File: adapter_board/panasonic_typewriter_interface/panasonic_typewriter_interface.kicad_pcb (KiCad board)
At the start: 2 copper layers, 37.3 x 43.7 mm, 21 parts, among them J1 KMDGX-8S-AS, J2 Conn_02x03_Odd_Even, J3 Connector:Conn_01x05_Male, J4 Connector:Conn_01x04_Male, J5 Connector:Conn_01x04_Male, SW1 SW_SPDT

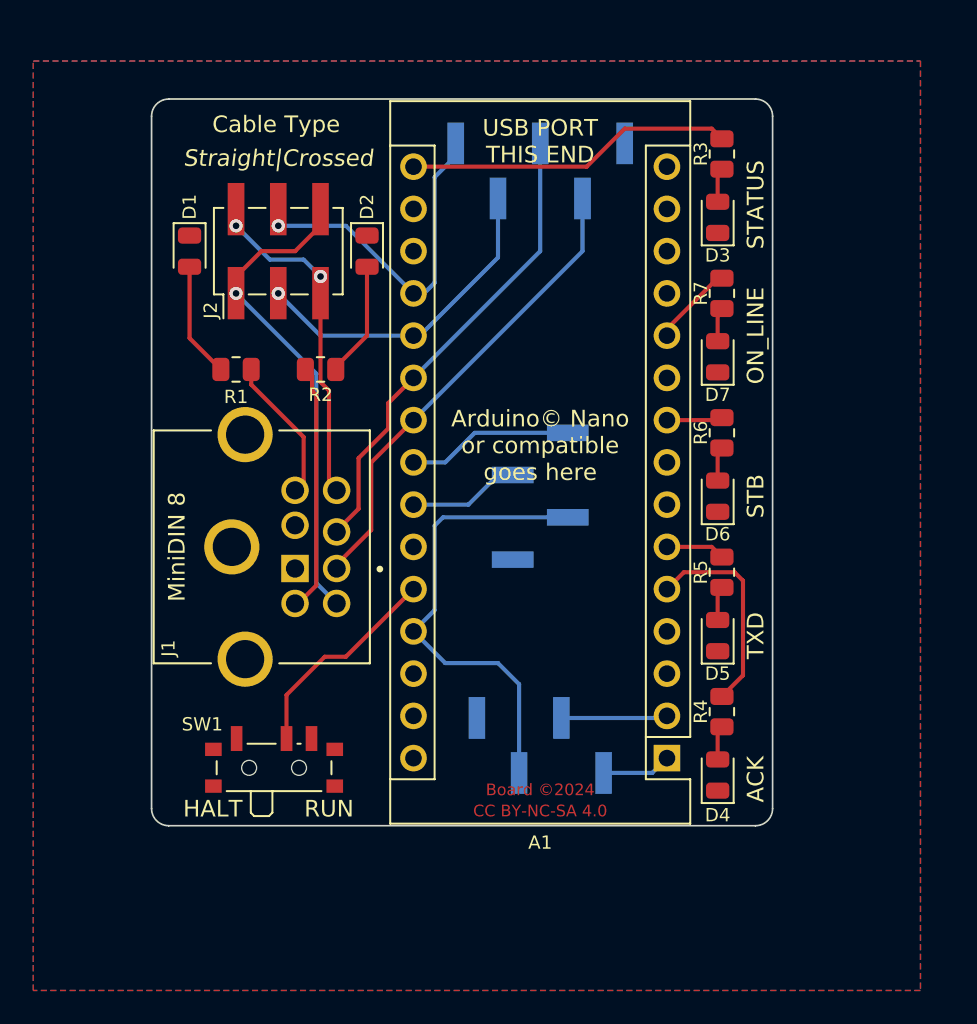
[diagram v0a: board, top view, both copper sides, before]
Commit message: slightly larger board with mounting holes and an extra button
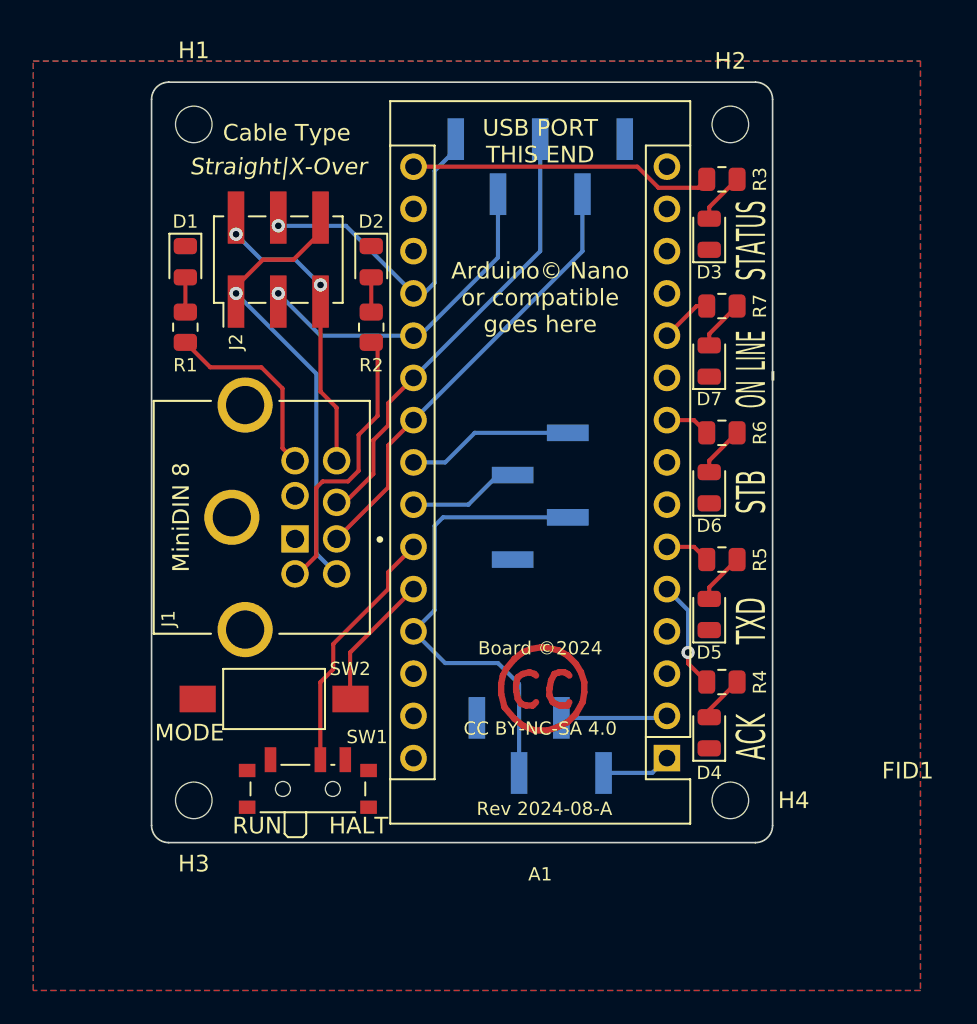
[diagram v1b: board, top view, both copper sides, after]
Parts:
- added FID1: CC, Symbol:Symbol_CreativeCommons_CopperTop_Type2_Small, F.Cu at (144.8, 102.6)
- added H1: MountingHole, MountingHole:MountingHole_2.2mm_M2_DIN965, F.Cu at (124.0, 68.6)
- added H2: MountingHole, MountingHole:MountingHole_2.2mm_M2_DIN965, F.Cu at (156.2, 68.6)
- added H3: MountingHole, MountingHole:MountingHole_2.2mm_M2_DIN965, F.Cu at (124.0, 109.2)
- added H4: MountingHole, MountingHole:MountingHole_2.2mm_M2_DIN965, F.Cu at (156.2, 109.2)
- added SW2: SW_Push, Button_Switch_SMD:SW_SPST_FSMSM, F.Cu at (128.8, 103.1)
- moved R1 3.97 mm to (123.4, 80.8), turned to 90 degrees
- moved R2 3.97 mm to (134.6, 80.8), turned to 90 degrees
- moved D4 2.59 mm to (154.9, 105.2)
- moved SW1 2.40 mm to (130.8, 108.2)
- moved J1 1.78 mm to (126.2, 92.2)
- moved R4 1.78 mm to (155.7, 102.1), turned to 0 degrees
- moved R3 1.52 mm to (155.7, 71.9), turned to 0 degrees
- moved D5 1.37 mm to (154.9, 98.0)
- moved D3 1.14 mm to (154.9, 75.2)
- moved R5 0.76 mm to (155.7, 94.7), turned to 0 degrees
- moved R7 0.76 mm to (155.7, 79.5), turned to 0 degrees
- moved D6 0.72 mm to (154.9, 90.4)
- moved D1 0.68 mm to (123.4, 76.8)
- moved D2 0.68 mm to (134.6, 76.8)
- moved D7 0.57 mm to (154.9, 82.8)
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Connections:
- A1 pad 25: unconnected-(A1-Pad25) -> GO_PIN
- A1 pad 26: GO_PIN -> MODE_PIN
- SW1 pad 1: unconnected-(SW1-Pad1) -> GND
- SW1 pad 3: GND -> unconnected-(SW1-Pad3)
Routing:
- net MODE_PIN: track 0.00 -> 8.19 mm
- net ACK_LED: track 12.7 -> 6.58 mm, vias 0 -> 1
- net Net-(D2-Pad2): track 6.95 -> 2.09 mm
- net Net-(R1-Pad2): track 6.95 -> 2.09 mm
- net +12V_CORRECT: track 8.79 -> 11.6 mm
- net DIN_6_TXD_OR_ON_LINE: track 29.5 -> 27.1 mm
- net +12V_CROSS: track 14.8 -> 17.1 mm
- net DIN_8_TXD_OR_ON_LINE: track 19.6 -> 17.3 mm
- net GO_PIN: track 12.9 -> 15.1 mm
- net ON_LINE_LED: track 4.97 -> 3.13 mm
- net ~{ACK}: track 28.4 -> 26.8 mm
- net STATUS_LED: track 19.7 -> 18.4 mm
- net ~{STB}: track 28.4 -> 27.2 mm
- net Net-(D7-Pad2): track 2.07 -> 3.06 mm
- net Net-(D6-Pad2): track 2.07 -> 3.06 mm
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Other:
- board size 37.3 x 43.7 mm -> 37.3 x 45.7 mm
- board text added: "Arduino Serial Breakout (TTL)"
- board text added: "Cable Type (J2): Move both jumpers on J2 to either STRAIGHT or X-OVER. If connecting KX-R, LEDs D1/D2 show current cable type but jumpers must still be moved to side closest to lit LED."
- board text added: "MODE"
- board text added: "Mounting Holes: Size: M2 Spacing: 40.6mm x 32.6mm"
- board text added: "Rev 2024-08-A"
- board text added: "Straight|X-Over"
- board text added: "Typewriter Signal Breakout (raw)"
- board text removed: "Arduino Serial0 Breakout"
- board text removed: "Cable Type jumper: Move BOTH J2 jumpers to either {dblquote}straight{dblquote} or {dblquote}crossed{dblquote}. If connecting to KX-R, LED will be lit indicating current cable type but jumpers MUST still be moved to side closest to lit LED."
- board text removed: "Straight|Crossed"
- board text removed: "Typewriter Signal Breakout"

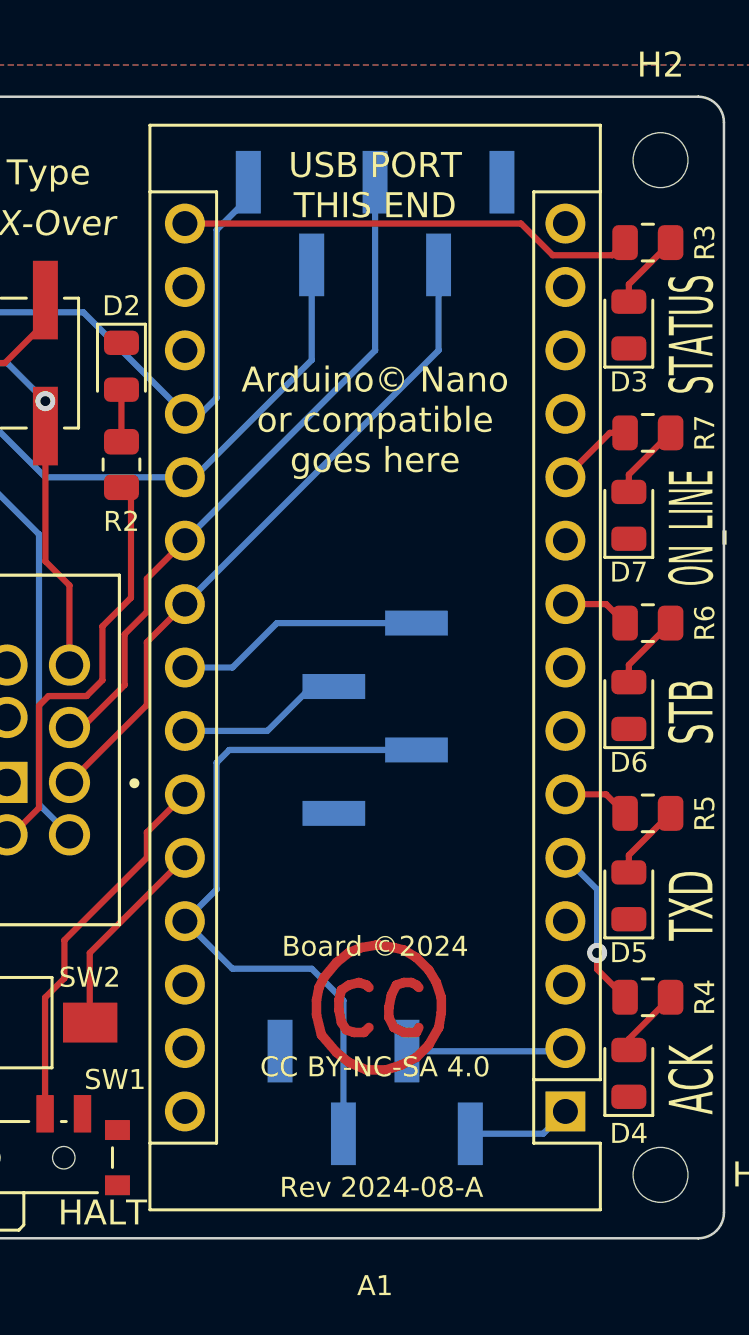
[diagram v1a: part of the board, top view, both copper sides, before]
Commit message: Add support for Serial1 on 328PB; change typewriter and serial breakouts to a JST 1.25 connector; changed i2c breakout to be a stemma-compatible jst-sh connector
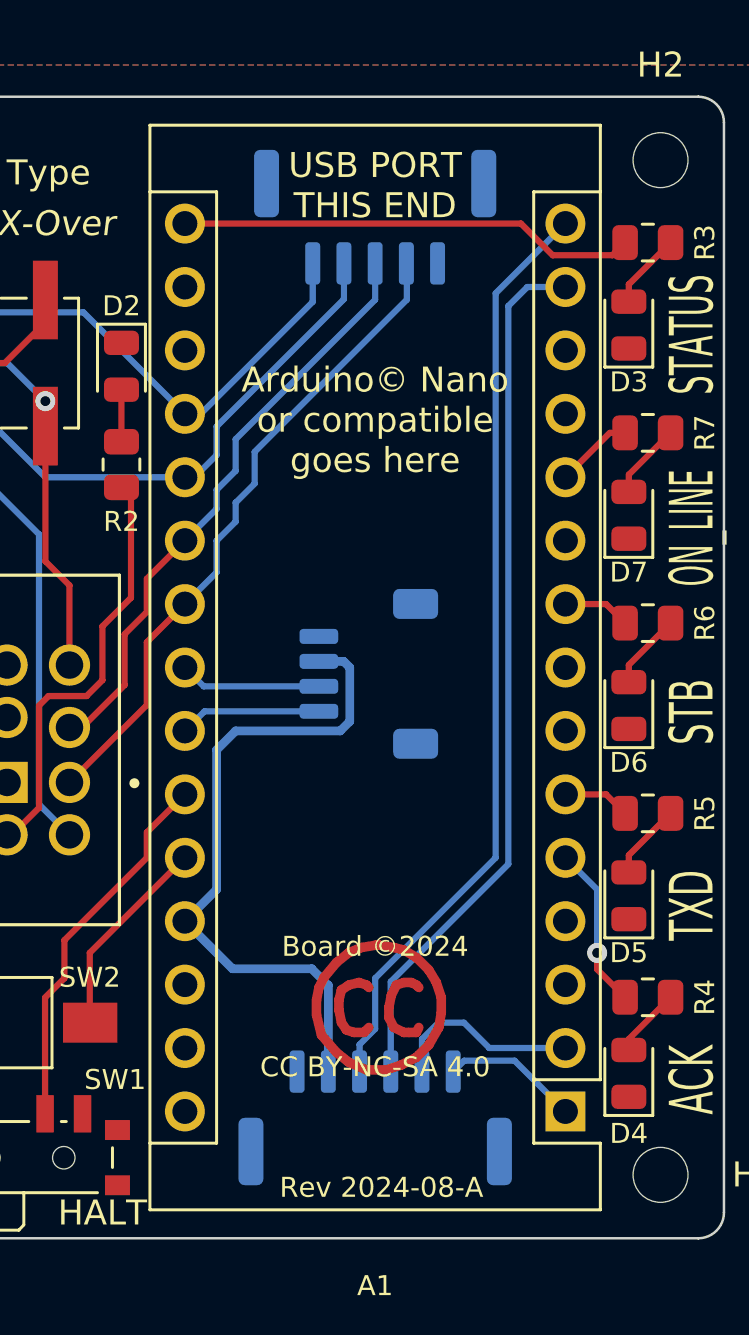
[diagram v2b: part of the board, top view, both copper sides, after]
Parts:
- J3: value Connector:Conn_01x05_Male -> Conn_01x05_MountingPin; footprint Connector_PinHeader_2.54mm:PinHeader_1x05_P2.54mm_Vertical_SMD_Pin1Left -> Connector_JST:JST_GH_SM05B-GHS-TB_1x05-1MP_P1.25mm_Horizontal
- J4: value Connector:Conn_01x04_Male -> Conn_01x06_MountingPin; footprint Connector_PinHeader_2.54mm:PinHeader_1x04_P2.54mm_Vertical_SMD_Pin1Left -> Connector_JST:JST_GH_SM06B-GHS-TB_1x06-1MP_P1.25mm_Horizontal
- J5: value Connector:Conn_01x04_Male -> Conn_01x04_MountingPin; footprint Connector_PinHeader_2.54mm:PinHeader_1x04_P2.54mm_Vertical_SMD_Pin1Left -> Connector_JST:JST_SH_SM04B-SRSS-TB_1x04-1MP_P1.00mm_Horizontal
- moved J5 1.80 mm to (144.5, 89.2), turned to -90 degrees
- moved J4 1.02 mm to (144.8, 106.9), turned to 180 degrees
- moved J3 0.25 mm to (144.8, 70.9), turned to 0 degrees
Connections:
- A1 pad 14: unconnected-(A1-Pad14) -> SERIAL1_TX
- A1 pad 15: unconnected-(A1-Pad15) -> SERIAL1_RX
- J4 pad 3: +5V -> SERIAL1_TX
- J4 pad 4: GND -> SERIAL1_RX
- J5 pad 1: SDA -> GND
- J5 pad 2: SCL -> +5V
- J5 pad 3: +5V -> SDA
- J5 pad 4: GND -> SCL
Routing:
- net SERIAL1_RX: track 0.00 -> 37.4 mm
- net SERIAL1_TX: track 0.00 -> 35.2 mm
- net SDA: track 10.0 -> 5.68 mm
- net ~{STB}: track 27.2 -> 24.0 mm
- net ~{ON_LINE}: track 21.0 -> 18.8 mm
- net SERIAL0_TX: track 4.18 -> 5.52 mm
- net SERIAL0_RX: track 6.40 -> 7.74 mm
- net +5V: track 28.1 -> 27.0 mm
- net SCL: track 6.70 -> 5.69 mm
- net TXD: track 20.5 -> 21.1 mm
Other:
- board text added: "Adafruit© Stemma QT compatible"
- board text added: "I^{2}C"
- board text added: "RX0"
- board text added: "RX1"
- board text added: "TX0"
- board text added: "TX1"
- board text added: "TX1/RX1: '328PB only"
- board text added: "Typewriter Signal Breakout"
- board text removed: "+5"
- board text removed: "I^{2}C Breakout"
- board text removed: "RX"
- board text removed: "TX"
- board text removed: "Typewriter Signal Breakout (raw)"

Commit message: misc updates
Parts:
- J3: value Conn_01x05_MountingPin -> Conn_01x06_MountingPin; footprint Connector_JST:JST_GH_SM05B-GHS-TB_1x05-1MP_P1.25mm_Horizontal -> Connector_JST:JST_GH_SM06B-GHS-TB_1x06-1MP_P1.25mm_Horizontal
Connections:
- J3 pad 5: GND -> +5V
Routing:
- net +5V: track 27.0 -> 50.1 mm
- net SERIAL0_RX: track 7.74 -> 7.02 mm
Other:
- board text added: "I routed +5V like this just to avoid using a few more vias!"
- board text added: "I router +5V this way just to avoid using 4 more vias"
